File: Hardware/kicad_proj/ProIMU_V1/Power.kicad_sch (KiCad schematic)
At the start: 15 parts

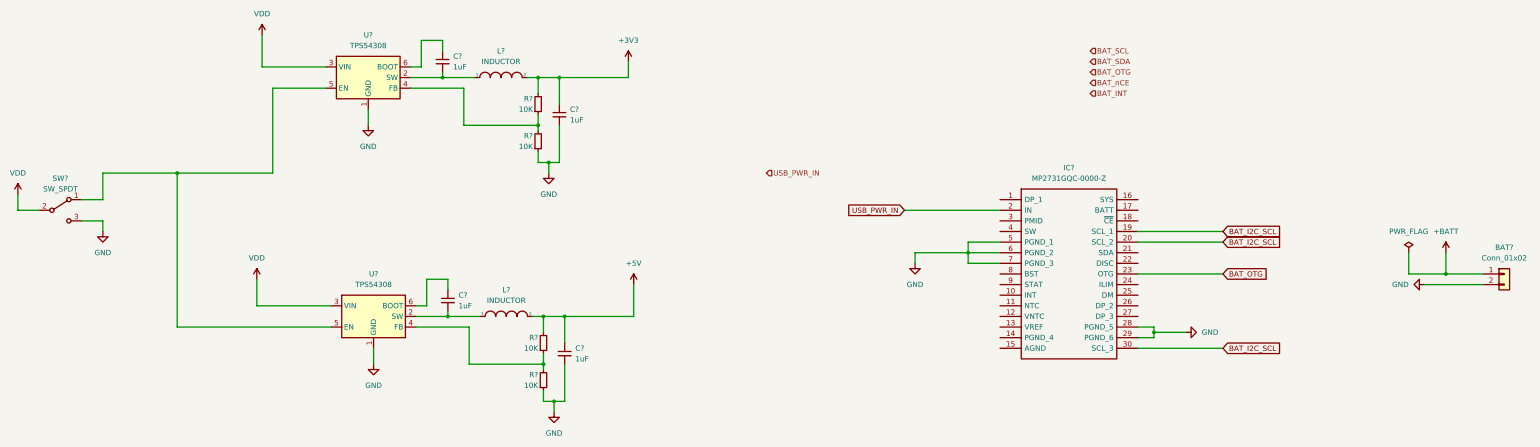
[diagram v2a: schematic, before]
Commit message: Layout Updated. CAN and RS485 section to be updated
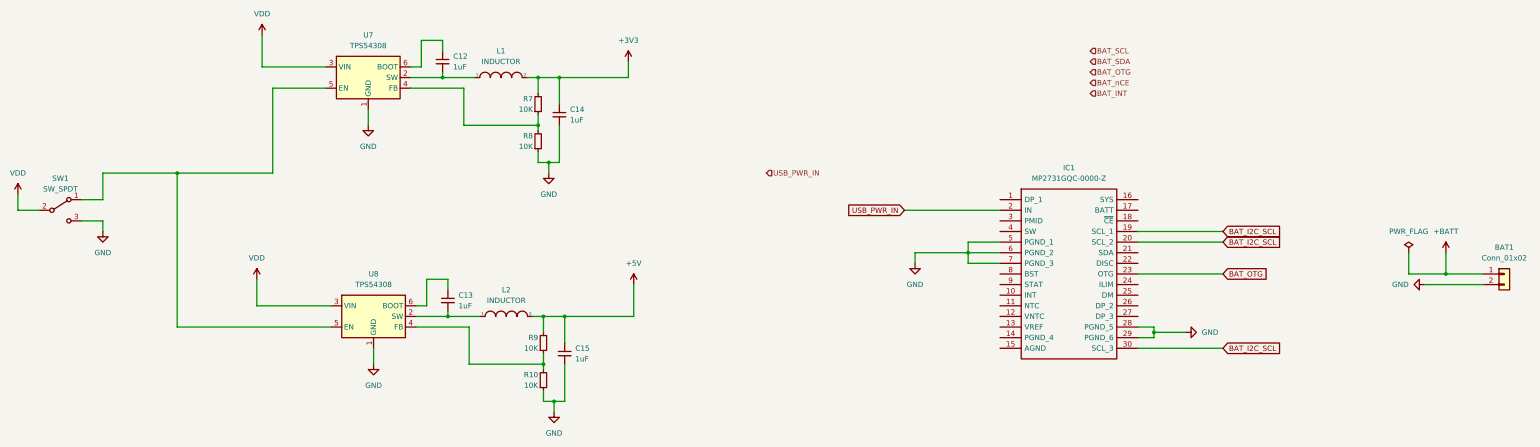
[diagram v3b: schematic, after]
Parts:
- gave numbers to parts that had none: 15
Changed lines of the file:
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@@
   (symbol (lib_id "pspice:INDUCTOR") (at 153.67 64.77 0) (unit 1)
     (in_bom yes) (on_board yes) (fields_autoplaced)
-    (property "Reference" "L?" (id 0) (at 153.67 58.42 0))
+    (property "Reference" "L1" (id 0) (at 153.67 58.42 0))
     (property "Value" "INDUCTOR" (id 1) (at 153.67 60.96 0))
     (property "Footprint" "" (id 2) (at 153.67 64.77 0)
@@
   (symbol (lib_id "power:VDD") (at 38.1 92.71 0) (unit 1)
     (in_bom yes) (on_board yes) (fields_autoplaced)
-    (property "Reference" "#PWR?" (id 0) (at 38.1 96.52 0)
+    (property "Reference" "#PWR041" (id 0) (at 38.1 96.52 0)
       (effects (font (size 1.27 1.27)) hide)
     )
@@
   (symbol (lib_id "Device:R_Small") (at 163.83 128.27 0) (mirror x) (unit 1)
     (in_bom yes) (on_board yes)
-    (property "Reference" "R?" (id 0) (at 162.56 127 0)
+    (property "Reference" "R9" (id 0) (at 162.56 127 0)
       (effects (font (size 1.27 1.27)) (justify right))
     )
@@
   (symbol (lib_id "Device:C_Small") (at 140.97 118.11 0) (unit 1)
     (in_bom yes) (on_board yes) (fields_autoplaced)
-    (property "Reference" "C?" (id 0) (at 143.51 116.8462 0)
+    (property "Reference" "C13" (id 0) (at 143.51 116.8462 0)
       (effects (font (size 1.27 1.27)) (justify left))
     )
@@
   (symbol (lib_id "power:GND") (at 123.19 133.35 0) (unit 1)
     (in_bom yes) (on_board yes) (fields_autoplaced)
-    (property "Reference" "#PWR?" (id 0) (at 123.19 139.7 0)
+    (property "Reference" "#PWR046" (id 0) (at 123.19 139.7 0)
       (effects (font (size 1.27 1.27)) hide)
     )
@@
   (symbol (lib_id "Device:R_Small") (at 162.56 71.12 0) (mirror x) (unit 1)
     (in_bom yes) (on_board yes)
-    (property "Reference" "R?" (id 0) (at 161.29 69.85 0)
+    (property "Reference" "R7" (id 0) (at 161.29 69.85 0)
       (effects (font (size 1.27 1.27)) (justify right))
     )
@@
   (symbol (lib_id "power:+3V3") (at 184.15 60.96 0) (unit 1)
     (in_bom yes) (on_board yes) (fields_autoplaced)
-    (property "Reference" "#PWR?" (id 0) (at 184.15 64.77 0)
+    (property "Reference" "#PWR049" (id 0) (at 184.15 64.77 0)
       (effects (font (size 1.27 1.27)) hide)
     )
@@
   (symbol (lib_id "power:+BATT") (at 379.73 106.68 0) (mirror y) (unit 1)
     (in_bom yes) (on_board yes) (fields_autoplaced)
-    (property "Reference" "#PWR?" (id 0) (at 379.73 110.49 0)
+    (property "Reference" "#PWR054" (id 0) (at 379.73 110.49 0)
       (effects (font (size 1.27 1.27)) hide)
     )
@@
   (symbol (lib_id "Device:C_Small") (at 167.64 73.66 0) (unit 1)
     (in_bom yes) (on_board yes) (fields_autoplaced)
-    (property "Reference" "C?" (id 0) (at 170.18 72.3962 0)
+    (property "Reference" "C14" (id 0) (at 170.18 72.3962 0)
       (effects (font (size 1.27 1.27)) (justify left))
     )
@@
   (symbol (lib_id "power:GND") (at 58.42 101.6 0) (unit 1)
     (in_bom yes) (on_board yes) (fields_autoplaced)
-    (property "Reference" "#PWR?" (id 0) (at 58.42 107.95 0)
+    (property "Reference" "#PWR042" (id 0) (at 58.42 107.95 0)
       (effects (font (size 1.27 1.27)) hide)
     )
@@
   (symbol (lib_id "Device:C_Small") (at 139.7 60.96 0) (unit 1)
     (in_bom yes) (on_board yes) (fields_autoplaced)
-    (property "Reference" "C?" (id 0) (at 142.24 59.6962 0)
+    (property "Reference" "C12" (id 0) (at 142.24 59.6962 0)
       (effects (font (size 1.27 1.27)) (justify left))
     )
@@
   (symbol (lib_id "power:GND") (at 165.1 87.63 0) (unit 1)
     (in_bom yes) (on_board yes) (fields_autoplaced)
-    (property "Reference" "#PWR?" (id 0) (at 165.1 93.98 0)
+    (property "Reference" "#PWR047" (id 0) (at 165.1 93.98 0)
       (effects (font (size 1.27 1.27)) hide)
     )
@@
   (symbol (lib_id "Regulator_Switching:TPS54308") (at 123.19 121.92 0) (unit 1)
     (in_bom yes) (on_board yes) (fields_autoplaced)
-    (property "Reference" "U?" (id 0) (at 123.19 111.76 0))
+    (property "Reference" "U8" (id 0) (at 123.19 111.76 0))
     (property "Value" "TPS54308" (id 1) (at 123.19 114.3 0))
     (property "Footprint" "Package_TO_SOT_SMD:SOT-23-6" (id 2) (at 124.46 130.81 0)
@@
   (symbol (lib_id "power:GND") (at 166.37 144.78 0) (unit 1)
     (in_bom yes) (on_board yes) (fields_autoplaced)
-    (property "Reference" "#PWR?" (id 0) (at 166.37 151.13 0)
+    (property "Reference" "#PWR048" (id 0) (at 166.37 151.13 0)
       (effects (font (size 1.27 1.27)) hide)
     )
@@
   (symbol (lib_id "Switch:SW_SPDT") (at 48.26 96.52 0) (unit 1)
     (in_bom yes) (on_board yes) (fields_autoplaced)
-    (property "Reference" "SW?" (id 0) (at 48.26 88.9 0))
+    (property "Reference" "SW1" (id 0) (at 48.26 88.9 0))
     (property "Value" "SW_SPDT" (id 1) (at 48.26 91.44 0))
     (property "Footprint" "" (id 2) (at 48.26 96.52 0)
@@
   (symbol (lib_id "power:GND") (at 317.5 125.73 90) (unit 1)
     (in_bom yes) (on_board yes) (fields_autoplaced)
-    (property "Reference" "#PWR?" (id 0) (at 323.85 125.73 0)
+    (property "Reference" "#PWR052" (id 0) (at 323.85 125.73 0)
       (effects (font (size 1.27 1.27)) hide)
     )
@@
   (symbol (lib_id "power:VDD") (at 95.25 113.03 0) (unit 1)
     (in_bom yes) (on_board yes) (fields_autoplaced)
-    (property "Reference" "#PWR?" (id 0) (at 95.25 116.84 0)
+    (property "Reference" "#PWR043" (id 0) (at 95.25 116.84 0)
       (effects (font (size 1.27 1.27)) hide)
     )
@@
   (symbol (lib_id "power:GND") (at 374.65 114.3 270) (mirror x) (unit 1)
     (in_bom yes) (on_board yes) (fields_autoplaced)
-    (property "Reference" "#PWR?" (id 0) (at 368.3 114.3 0)
+    (property "Reference" "#PWR053" (id 0) (at 368.3 114.3 0)
       (effects (font (size 1.27 1.27)) hide)
     )
@@
   (symbol (lib_id "Device:R_Small") (at 163.83 137.16 0) (mirror x) (unit 1)
     (in_bom yes) (on_board yes)
-    (property "Reference" "R?" (id 0) (at 162.56 135.89 0)
+    (property "Reference" "R10" (id 0) (at 162.56 135.89 0)
       (effects (font (size 1.27 1.27)) (justify right))
     )
@@
   (symbol (lib_id "power:VDD") (at 96.52 54.61 0) (unit 1)
     (in_bom yes) (on_board yes) (fields_autoplaced)
-    (property "Reference" "#PWR?" (id 0) (at 96.52 58.42 0)
+    (property "Reference" "#PWR044" (id 0) (at 96.52 58.42 0)
       (effects (font (size 1.27 1.27)) hide)
     )
@@
   (symbol (lib_id "Device:R_Small") (at 162.56 80.01 0) (mirror x) (unit 1)
     (in_bom yes) (on_board yes)
-    (property "Reference" "R?" (id 0) (at 161.29 78.74 0)
+    (property "Reference" "R8" (id 0) (at 161.29 78.74 0)
       (effects (font (size 1.27 1.27)) (justify right))
     )
@@
   (symbol (lib_id "Device:C_Small") (at 168.91 130.81 0) (unit 1)
     (in_bom yes) (on_board yes) (fields_autoplaced)
-    (property "Reference" "C?" (id 0) (at 171.45 129.5462 0)
+    (property "Reference" "C15" (id 0) (at 171.45 129.5462 0)
       (effects (font (size 1.27 1.27)) (justify left))
     )
@@
   (symbol (lib_id "power:+5V") (at 185.42 114.3 0) (unit 1)
     (in_bom yes) (on_board yes) (fields_autoplaced)
-    (property "Reference" "#PWR?" (id 0) (at 185.42 118.11 0)
+    (property "Reference" "#PWR050" (id 0) (at 185.42 118.11 0)
       (effects (font (size 1.27 1.27)) hide)
     )
@@
   (symbol (lib_id "Regulator_Switching:TPS54308") (at 121.92 64.77 0) (unit 1)
     (in_bom yes) (on_board yes) (fields_autoplaced)
-    (property "Reference" "U?" (id 0) (at 121.92 54.61 0))
+    (property "Reference" "U7" (id 0) (at 121.92 54.61 0))
     (property "Value" "TPS54308" (id 1) (at 121.92 57.15 0))
     (property "Footprint" "Package_TO_SOT_SMD:SOT-23-6" (id 2) (at 123.19 73.66 0)
@@
   (symbol (lib_id "MP2731GQC-0000-Z:MP2731GQC-0000-Z") (at 273.05 93.98 0) (unit 1)
     (in_bom yes) (on_board yes) (fields_autoplaced)
-    (property "Reference" "IC?" (id 0) (at 289.56 86.36 0))
+    (property "Reference" "IC1" (id 0) (at 289.56 86.36 0))
     (property "Value" "MP2731GQC-0000-Z" (id 1) (at 289.56 88.9 0))
     (property "Footprint" "footprints:MP2731GQC0000Z" (id 2) (at 302.26 91.44 0)
@@
   (symbol (lib_id "Connector_Generic:Conn_01x02") (at 393.7 111.76 0) (unit 1)
     (in_bom yes) (on_board yes) (fields_autoplaced)
-    (property "Reference" "BAT?" (id 0) (at 393.7 105.41 0))
+    (property "Reference" "BAT1" (id 0) (at 393.7 105.41 0))
     (property "Value" "Conn_01x02" (id 1) (at 393.7 107.95 0))
     (property "Footprint" "Connector_PinSocket_2.54mm:PinSocket_1x02_P2.54mm_Vertical" (id 2) (at 393.7 111.76 0)
@@
   (symbol (lib_id "power:GND") (at 121.92 76.2 0) (unit 1)
     (in_bom yes) (on_board yes) (fields_autoplaced)
-    (property "Reference" "#PWR?" (id 0) (at 121.92 82.55 0)
+    (property "Reference" "#PWR045" (id 0) (at 121.92 82.55 0)
       (effects (font (size 1.27 1.27)) hide)
     )
@@
   (symbol (lib_id "power:GND") (at 252.73 109.22 0) (unit 1)
     (in_bom yes) (on_board yes) (fields_autoplaced)
-    (property "Reference" "#PWR?" (id 0) (at 252.73 115.57 0)
+    (property "Reference" "#PWR051" (id 0) (at 252.73 115.57 0)
       (effects (font (size 1.27 1.27)) hide)
     )
@@
   (symbol (lib_id "pspice:INDUCTOR") (at 154.94 121.92 0) (unit 1)
     (in_bom yes) (on_board yes) (fields_autoplaced)
-    (property "Reference" "L?" (id 0) (at 154.94 115.57 0))
+    (property "Reference" "L2" (id 0) (at 154.94 115.57 0))
     (property "Value" "INDUCTOR" (id 1) (at 154.94 118.11 0))
     (property "Footprint" "" (id 2) (at 154.94 121.92 0)
@@
   (symbol (lib_id "power:PWR_FLAG") (at 370.84 106.68 0) (mirror y) (unit 1)
     (in_bom yes) (on_board yes) (fields_autoplaced)
-    (property "Reference" "#FLG?" (id 0) (at 370.84 104.775 0)
-      (effects (font (size 1.27 1.27)) hide)
-    )
+    (property "Reference" "#FLG01" (id 0) (at 370.84 104.775 0)
+      (effects (font (size 1.27 1.27)) hide)
+    )

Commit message: Updated Schematic and Layout
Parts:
- added C23, C25, C26, C28: 1uF, Capacitor_SMD:C_0402_1005Metric_Pad0.74x0.62mm_HandSolder, symbol Device:C_Small
- added C24, C27: 10uF, Capacitor_SMD:C_0402_1005Metric_Pad0.74x0.62mm_HandSolder, symbol Device:C_Small
- added D2: LED, LED_SMD:LED_0603_1608Metric, symbol Device:LED
- added L3: 1.0uH, Inductor_SMD:L_0805_2012Metric_Pad1.05x1.20mm_HandSolder, symbol Device:L
- added Q1: 2SC4213, Package_TO_SOT_SMD:SOT-323_SC-70, symbol Transistor_BJT:2SC4213
- added R14, R17, R19: 10K, Resistor_SMD:R_0402_1005Metric_Pad0.72x0.64mm_HandSolder, symbol Device:R_Small
- added R15, R16, R18: 1K, Resistor_SMD:R_0402_1005Metric_Pad0.72x0.64mm_HandSolder, symbol Device:R_Small
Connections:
- net +BATT is gone; now on net BATT: BAT1.1 (Pin_1)
- net GND: now also IC1.14 (PGND_4), IC1.15 (AGND), C23.2, C24.2, C25.2, C26.2, C27.2, Q1.2 (E), R14.1; no longer BAT1.2 (Pin_2)
- net DP: now reaches IC1.1 (DP_1)
- net DP: now also IC1.26 (DP_2), IC1.27 (DP_3)
- net INT: now reaches IC1.10 (INT)
- net NTC: now reaches IC1.11 (NTC)
- net NTC: now also R15.2, R18.1
- net VNTC: now reaches IC1.12 (VNTC)
- net VNTC: now also R18.2
- net VREF: now reaches IC1.13 (VREF)
- net VREF: now also C24.1, R17.2, R19.2
- net SYS: now reaches IC1.16 (SYS)
- net SYS: now also C25.1, L3.1
- net BATT: now reaches IC1.17 (BATT)
- net BATT: now also C26.1
- net nCE: now reaches IC1.18 (~{CE})
- net SDA: now reaches IC1.21 (SDA)
- net DISC: now reaches IC1.22 (DISC)
- net DISC: now also Q1.3 (C), R19.1
- net ILIM: now reaches IC1.24 (ILIM)
- net ILIM: now also R14.2
- net DM: now reaches IC1.25 (DM)
- net PMID: now reaches IC1.3 (PMID)
- net PMID: now also C27.1
- net SW: now reaches IC1.4 (SW)
- net SW: now also C28.2, L3.2
- net BST: now reaches IC1.8 (BST)
- net BST: now also C28.1
- net STAT: now reaches IC1.9 (STAT)
- net STAT: now also D2.1 (K)
- net BAT_I2C_SCL renamed SCL
- net BAT_OTG renamed OTG
- net USB_PWR_IN renamed IN
- net IN: now also C23.1
- new net: Q1.1 (B), R16.2
- new net: BAT1.2 (Pin_2), R15.1
- new net: D2.2 (A), R17.1
- new net DISC_PIN: R16.1
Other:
- moved on the sheet: BAT1, C12, C13, C14, C15, IC1, L1, L2, R10, R7, R8, R9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

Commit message: Updated Schematic
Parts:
- removed BAT1: Conn_01x02, Connector_PinSocket_2.54mm:PinSocket_1x02_P2.54mm_Vertical, symbol Connector_Generic:Conn_01x02
- removed C23, C25, C26, C28: 1uF, Capacitor_SMD:C_0402_1005Metric_Pad0.74x0.62mm_HandSolder, symbol Device:C_Small
- removed C24, C27: 10uF, Capacitor_SMD:C_0402_1005Metric_Pad0.74x0.62mm_HandSolder, symbol Device:C_Small
- removed D2: LED, LED_SMD:LED_0603_1608Metric, symbol Device:LED
- removed IC1: MP2731GQC-0000-Z, footprints:MP2731GQC0000Z, symbol MP2731GQC-0000-Z:MP2731GQC-0000-Z
- removed L3: 1.0uH, Inductor_SMD:L_0805_2012Metric_Pad1.05x1.20mm_HandSolder, symbol Device:L
- removed Q1: 2SC4213, Package_TO_SOT_SMD:SOT-323_SC-70, symbol Transistor_BJT:2SC4213
- removed R14, R17, R19: 10K, Resistor_SMD:R_0402_1005Metric_Pad0.72x0.64mm_HandSolder, symbol Device:R_Small
- removed R15, R16, R18: 1K, Resistor_SMD:R_0402_1005Metric_Pad0.72x0.64mm_HandSolder, symbol Device:R_Small
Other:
- moved on the sheet: C12, C13, C14, C15, L1, L2, R10, R7, R8, R9, SW1, U7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

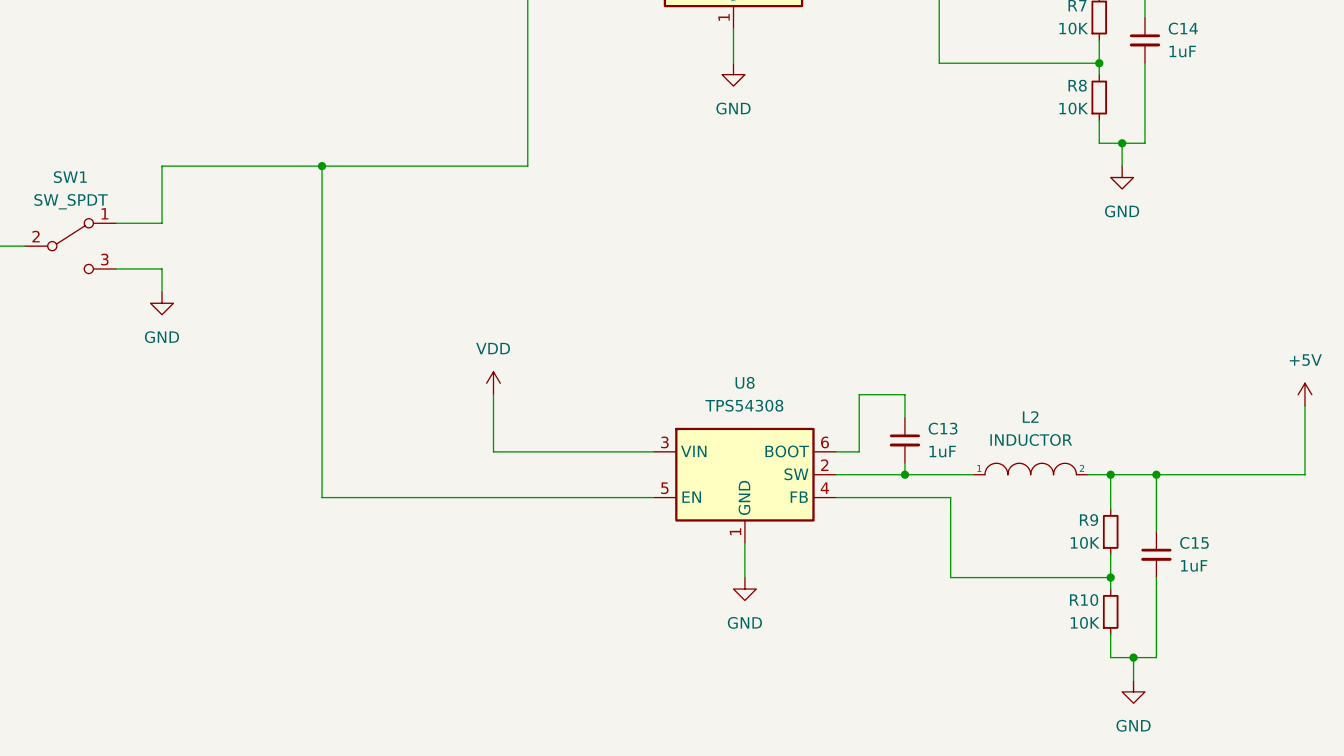
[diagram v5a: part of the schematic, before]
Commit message: Updated Layout, schematic, added new symbol and footprint
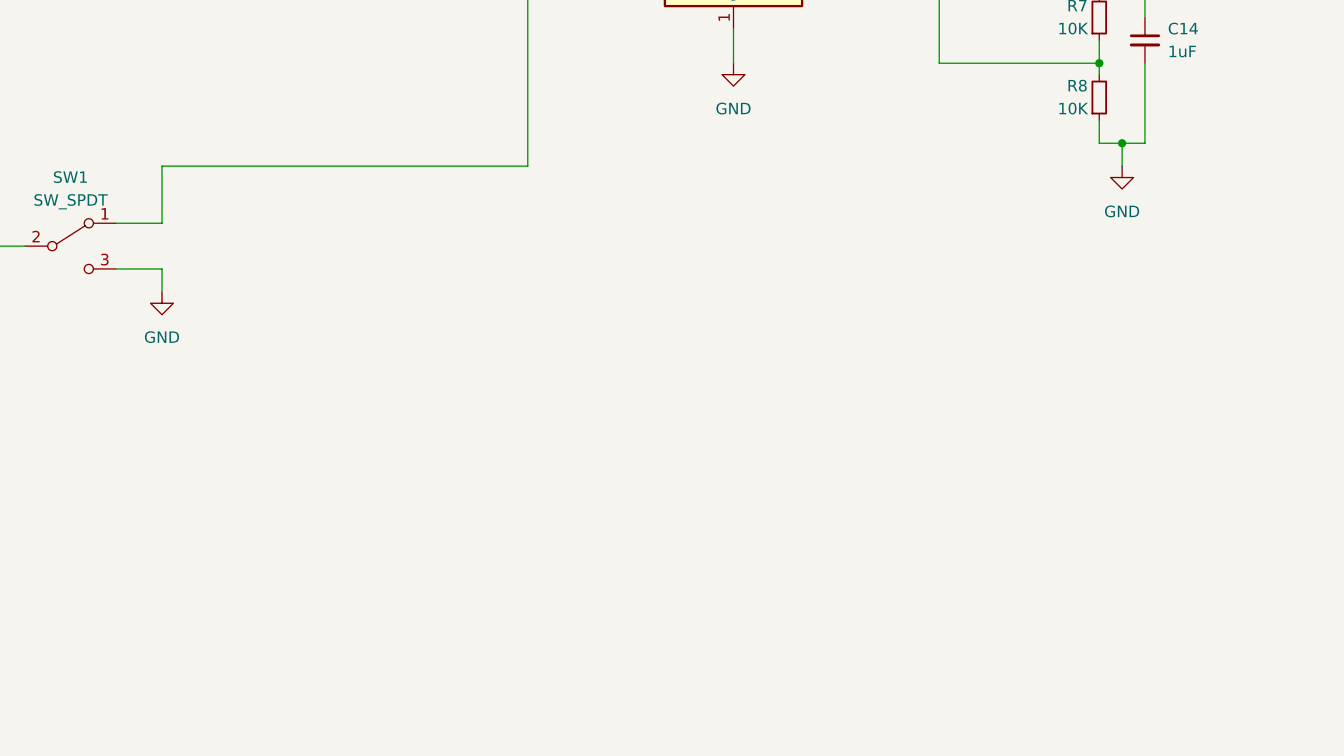
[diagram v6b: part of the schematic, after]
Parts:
- removed C13, C15: 1uF, Capacitor_SMD:C_0402_1005Metric_Pad0.74x0.62mm_HandSolder, symbol Device:C_Small
- removed L2: INDUCTOR, symbol pspice:INDUCTOR
- removed R10, R9: 10K, Resistor_SMD:R_0402_1005Metric_Pad0.72x0.64mm_HandSolder, symbol Device:R_Small
- removed U8: TPS54308, Package_TO_SOT_SMD:SOT-23-6, symbol Regulator_Switching:TPS54308
